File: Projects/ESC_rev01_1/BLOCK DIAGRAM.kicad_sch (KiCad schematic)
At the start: 0 parts

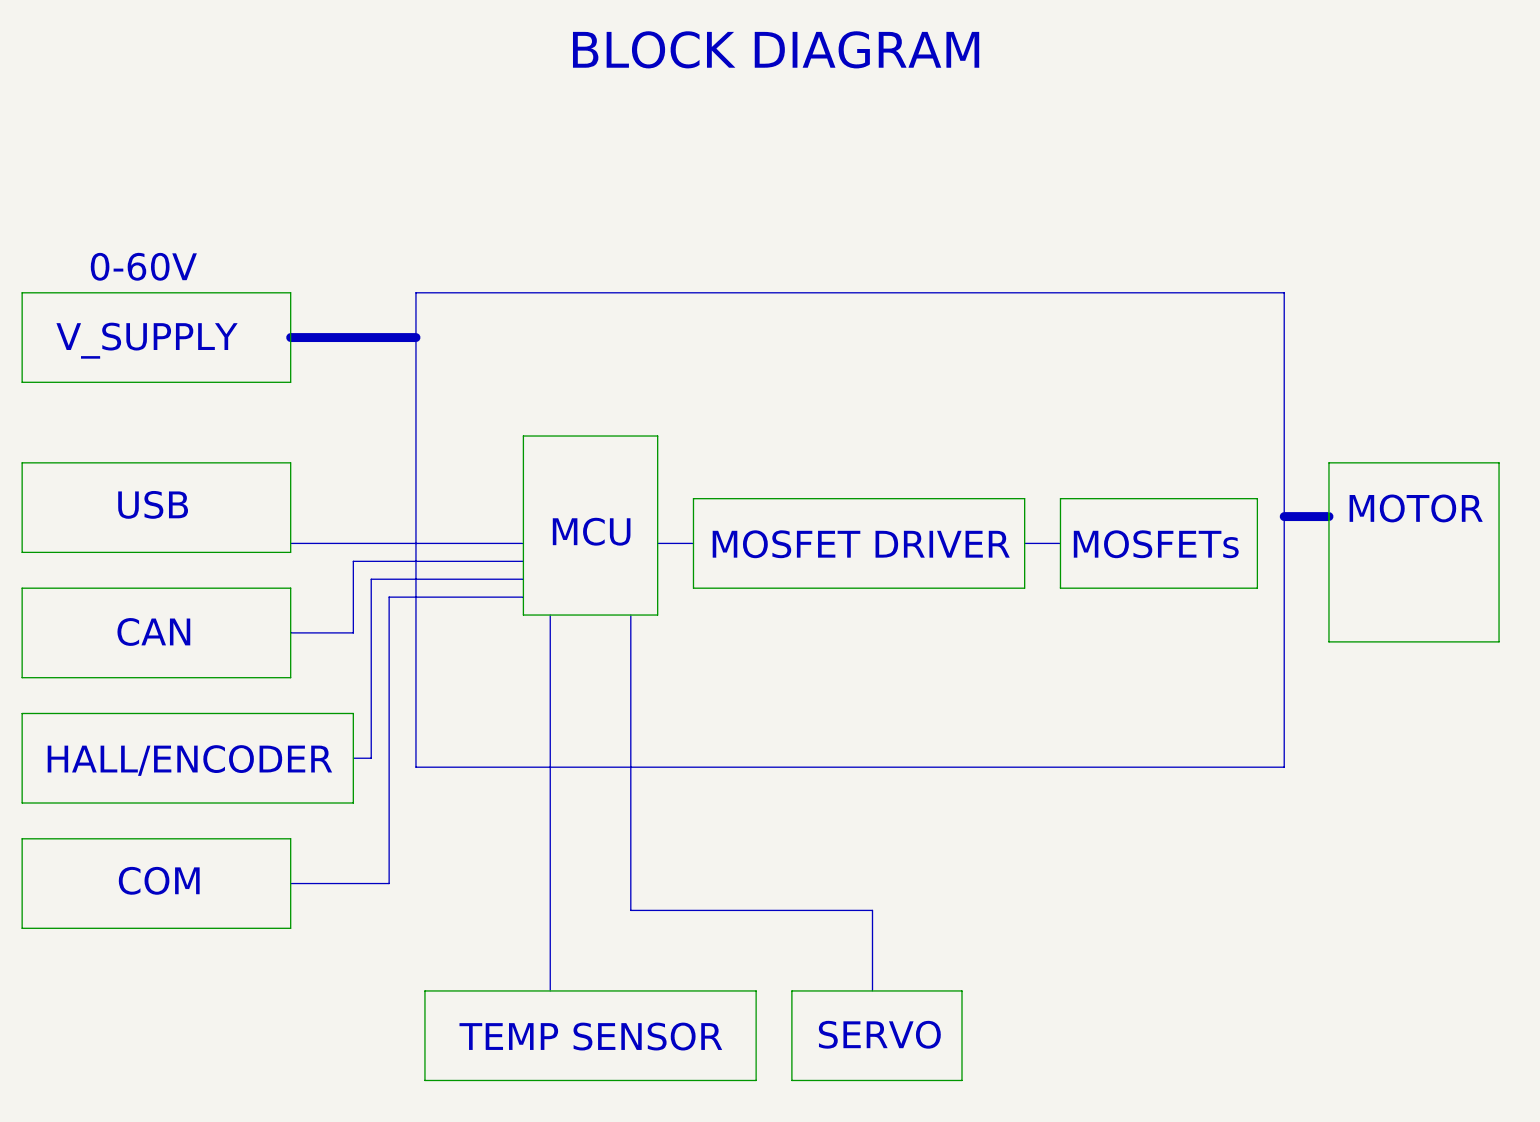
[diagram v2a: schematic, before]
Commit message: Update 07
Schematic is ready
INPUT PROTECTION schematic created
MOSFETs schematic created
CAN schematic created
FILTERs schematic created
MECHANICAL schematic created
STEP-DOWN schematic created
Footprints, 3D models are added and corrected (major issues)
Component placement started
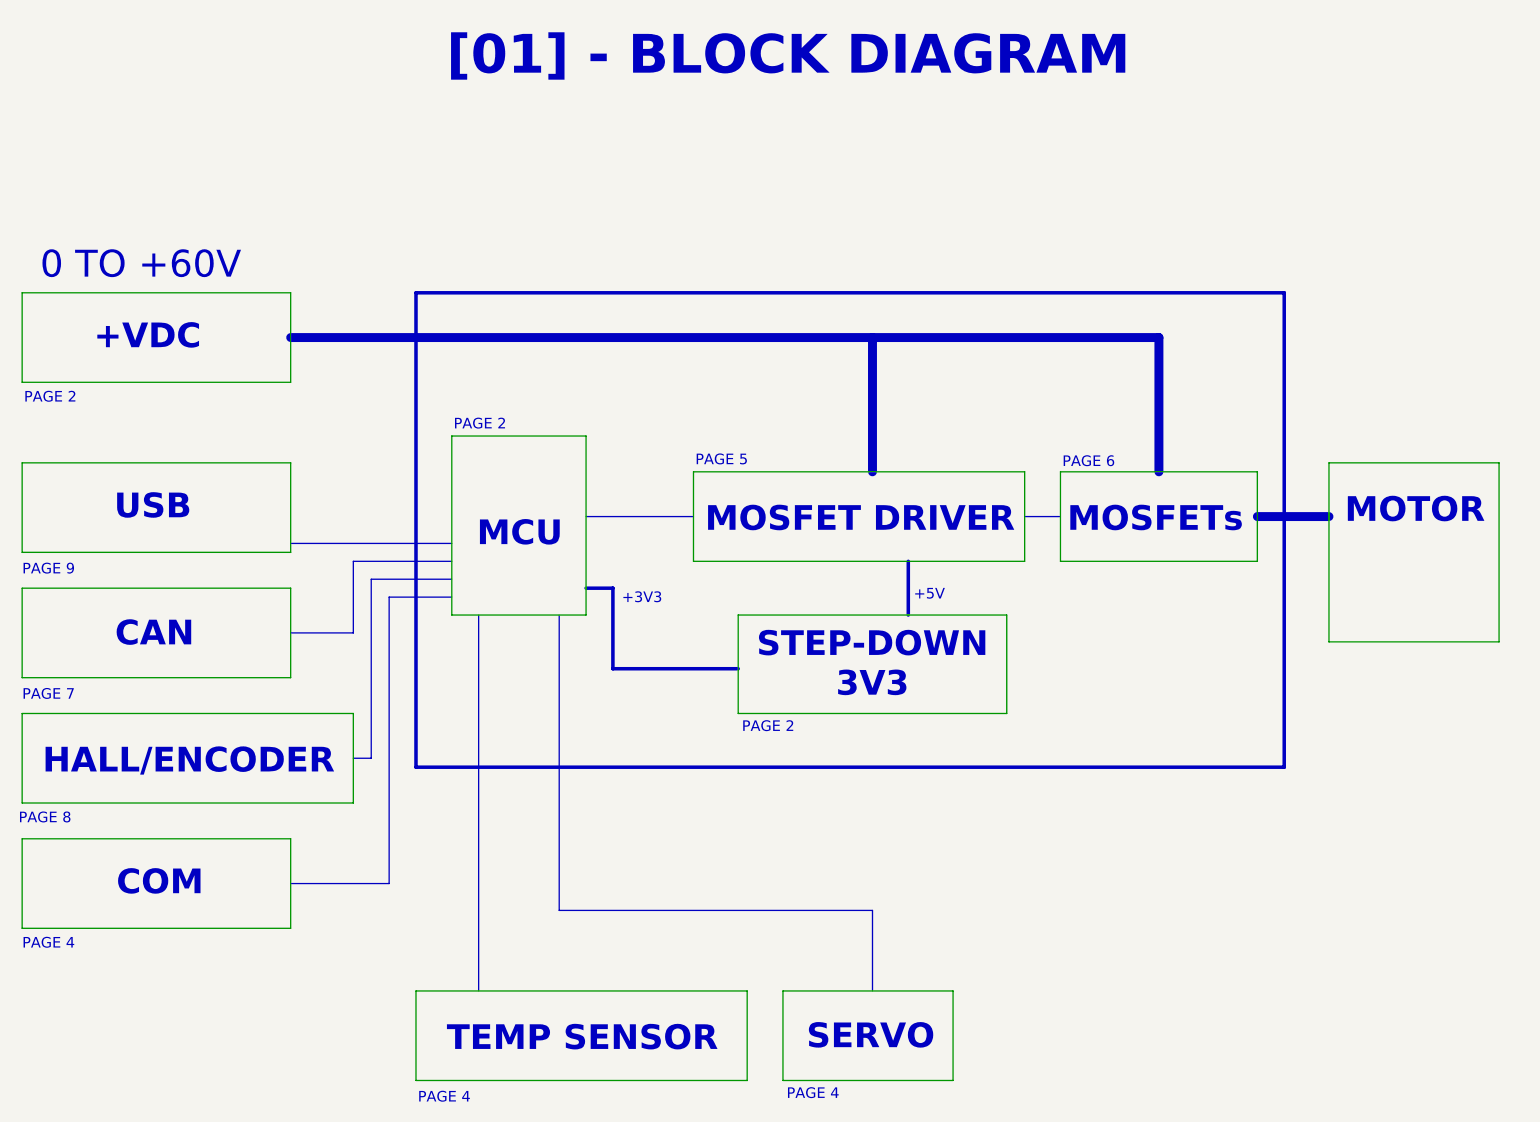
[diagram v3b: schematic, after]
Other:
- note added: "+3V3"
- note added: "+5V"
- note added: "+VDC"
- note added: "0 TO +60V"
- note added: "PAGE 2"
- note added: "PAGE 4"
- note added: "PAGE 5"
- note added: "PAGE 6"
- note added: "PAGE 7"
- note added: "PAGE 8"
- note added: "PAGE 9"
- note added: "STEP-DOWN 3V3"
- note added: "[01] - BLOCK DIAGRAM"
- note removed: "0-60V"
- note removed: "BLOCK DIAGRAM"
- note removed: "V_SUPPLY"

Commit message: Update 01
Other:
- title: (none) -> DF_ESC_rev01_1
